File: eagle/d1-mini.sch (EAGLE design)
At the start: 4 parts, among them J1 282834-2

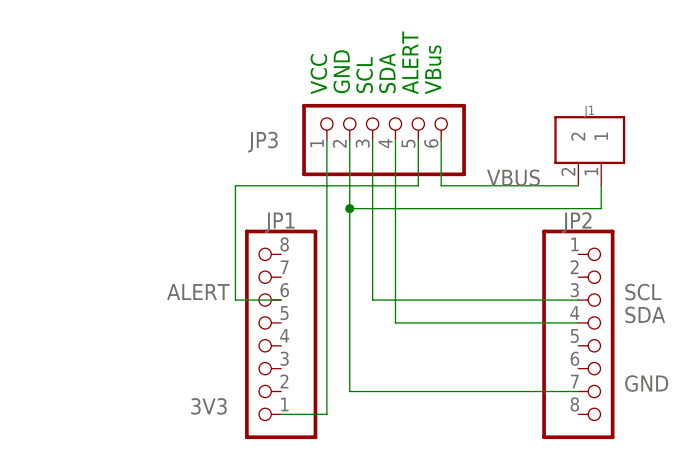
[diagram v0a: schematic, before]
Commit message: switch d1-mini eagle board to use 2.54mm pin header for vbus/gnd and add text/oshw logo
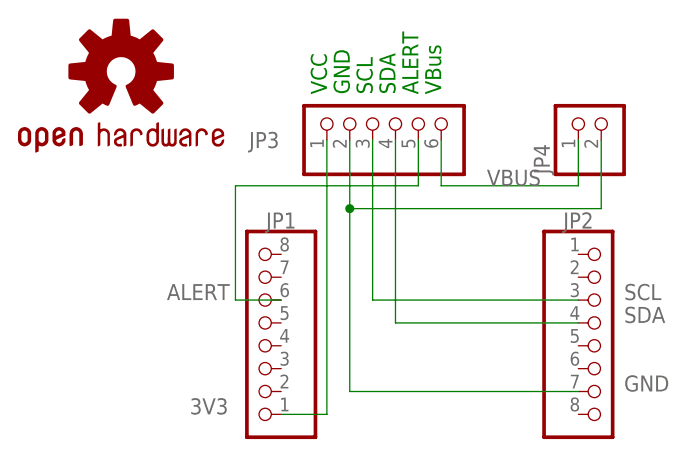
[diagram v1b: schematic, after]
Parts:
- removed J1: 282834-2, 282834-2:282834-2
- added JP4: (no value), pinhead:PINHD-1X2/90
- added LOGO1: OSHW-LOGOS, SparkFun-Aesthetics:OSHW-LOGOS
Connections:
- net GND: now also JP4.2; no longer J1.1
- net VBUS: now also JP4.1; no longer J1.2
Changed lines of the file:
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@@
 <layer number="136" name="silktop" color="7" fill="1" visible="yes" active="yes"/>
 <layer number="137" name="silkbottom" color="7" fill="1" visible="yes" active="yes"/>
+<layer number="138" name="EEE" color="7" fill="1" visible="no" active="no"/>
+<layer number="139" name="_tKeepout" color="7" fill="1" visible="no" active="no"/>
+<layer number="140" name="mbKeepout" color="7" fill="1" visible="no" active="no"/>
+<layer number="141" name="ASSEMBLY_TOP" color="7" fill="1" visible="no" active="no"/>
+<layer number="142" name="mbRestrict" color="7" fill="1" visible="no" active="no"/>
+<layer number="143" name="PLACE_BOUND_TOP" color="7" fill="1" visible="no" active="no"/>
 <layer number="144" name="Drill_legend" color="7" fill="1" visible="yes" active="yes"/>
 <layer number="145" name="DrillLegend_01-16" color="7" fill="1" visible="yes" active="yes"/>
 <layer number="146" name="DrillLegend_01-20" color="7" fill="1" visible="yes" active="yes"/>
+<layer number="147" name="PIN_NUMBER" color="7" fill="1" visible="no" active="no"/>
+<layer number="149" name="DrillLegend_02-15" color="7" fill="1" visible="no" active="no"/>
 <layer number="150" name="Notes" color="7" fill="1" visible="yes" active="yes"/>
 <layer number="151" name="HeatSink" color="7" fill="1" visible="yes" active="yes"/>
@@
 <layer number="166" name="AntennaArea" color="7" fill="1" visible="yes" active="yes"/>
 <layer number="168" name="4mmHeightArea" color="7" fill="1" visible="yes" active="yes"/>
+<layer number="191" name="mNets" color="7" fill="1" visible="no" active="no"/>
+<layer number="192" name="mBusses" color="7" fill="1" visible="no" active="no"/>
+<layer number="193" name="mPins" color="7" fill="1" visible="no" active="no"/>
+<layer number="194" name="mSymbols" color="7" fill="1" visible="no" active="no"/>
+<layer number="195" name="mNames" color="7" fill="1" visible="no" active="no"/>
+<layer number="196" name="mValues" color="7" fill="1" visible="no" active="no"/>
 <layer number="199" name="Contour" color="7" fill="1" visible="yes" active="yes"/>
 <layer number="200" name="200bmp" color="1" fill="10" visible="yes" active="yes"/>
@@
 <class number="0" name="default" width="0" drill="0">
 </class>
-<class number="1" name="current" width="0.254" drill="0">
+<class number="1" name="current" width="0.2" drill="0">
 </class>
-<class number="2" name="signal" width="0.00635" drill="0">
+<class number="2" name="signal" width="0.25" drill="0">
 </class>
 </classes>
@@
 <part name="JP2" library="pinhead" library_urn="urn:adsk.eagle:library:325" deviceset="PINHD-1X8" device="" package3d_urn="urn:adsk.eagle:package:22409/2"/>
 <part name="JP3" library="pinhead" library_urn="urn:adsk.eagle:library:325" deviceset="PINHD-1X6" device="" package3d_urn="urn:adsk.eagle:package:22472/2"/>
-<part name="J1" library="282834-2" deviceset="282834-2" device="" override_package3d_urn="urn:adsk.eagle:package:30793796/2" override_package_urn="urn:adsk.eagle:footprint:30793797/1" value=""/>
+<part name="JP4" library="pinhead" library_urn="urn:adsk.eagle:library:325" deviceset="PINHD-1X2" device="/90" package3d_urn="urn:adsk.eagle:package:22437/2"/>
+<part name="LOGO1" library="SparkFun-Aesthetics" deviceset="OSHW-LOGO" device="S"/>
 </parts>
 <sheets>
@@
 <attribute name="VALUE" x="53.34" y="74.93" size="1.778" layer="96" rot="R90"/>
 </instance>
-<instance part="J1" gate="G$1" x="63.5" y="78.74" smashed="yes" rot="R270">
-<attribute name="NAME" x="62.23" y="81.534" size="1.01741875" layer="95" align="bottom-center"/>
-<attribute name="VALUE" x="56.7619" y="81.79121875" size="1.01706875" layer="96" rot="R270"/>
-</instance>
+<instance part="JP4" gate="G$1" x="63.5" y="81.28" smashed="yes" rot="R90">
+<attribute name="NAME" x="57.785" y="74.93" size="1.778" layer="95" rot="R90"/>
+<attribute name="VALUE" x="68.58" y="74.93" size="1.778" layer="96" rot="R90"/>
+</instance>
+<instance part="LOGO1" gate="G$1" x="10.16" y="86.36" smashed="yes"/>
 </instances>
 <busses>
@@
 <wire x1="35.56" y1="71.12" x2="35.56" y2="50.8" width="0.1524" layer="91"/>
 <wire x1="35.56" y1="50.8" x2="60.96" y2="50.8" width="0.1524" layer="91"/>
-<pinref part="J1" gate="G$1" pin="1"/>
 <wire x1="35.56" y1="71.12" x2="63.5" y2="71.12" width="0.1524" layer="91"/>
-<wire x1="63.5" y1="71.12" x2="63.5" y2="73.66" width="0.1524" layer="91"/>
 <junction x="35.56" y="71.12"/>
+<pinref part="JP4" gate="G$1" pin="2"/>
+<wire x1="63.5" y1="71.12" x2="63.5" y2="78.74" width="0.1524" layer="91"/>
 </segment>
 </net>
@@
 <pinref part="JP3" gate="A" pin="6"/>
 <wire x1="45.72" y1="78.74" x2="45.72" y2="73.66" width="0.1524" layer="91"/>
-<pinref part="J1" gate="G$1" pin="2"/>
+<label x="50.8" y="73.66" size="1.778" layer="95"/>
+<pinref part="JP4" gate="G$1" pin="1"/>
 <wire x1="45.72" y1="73.66" x2="60.96" y2="73.66" width="0.1524" layer="91"/>
-<label x="50.8" y="73.66" size="1.778" layer="95"/>
+<wire x1="60.96" y1="73.66" x2="60.96" y2="78.74" width="0.1524" layer="91"/>
 </segment>
 </net>
@@
 </sheet>
 </sheets>
+<errors>
+</errors>
 </schematic>
 </drawing>
@@
 packages will not be understood (or retained) with this version.
 </note>
-<note version="9.4" severity="warning">
-Since Version 9.4, EAGLE supports the overriding of 3D packages
-in schematics and board files. Those overridden 3d packages
-will not be understood (or retained) with this version.
-</note>
 </compatibility>
